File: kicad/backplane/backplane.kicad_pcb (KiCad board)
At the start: 2 copper layers, 190.5 x 105 mm, 56 parts, among them J1 Board Connector, J2 Board Connector, J3 Board Connector, J4 Board Connector, J5 Board Connector, J6 Board Connector, J7 Board Connector, J8 Conn_02x04_Counter_Clockwise, J9 Screw_Terminal_01x02, SW1 SW_SPDT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

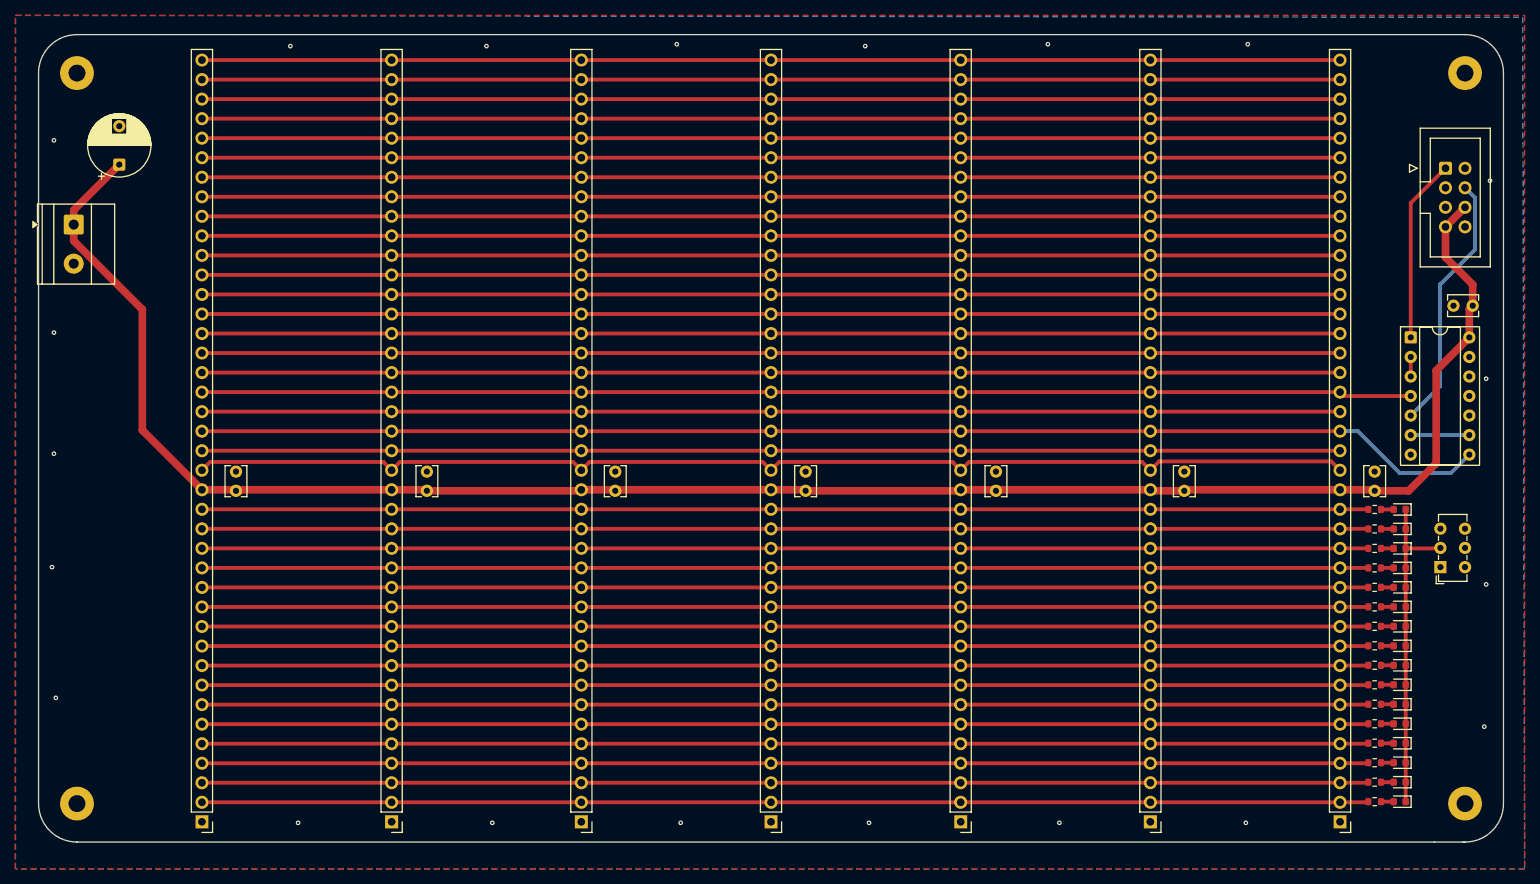
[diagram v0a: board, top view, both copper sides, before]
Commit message: integrated wozmon, updated kicad to specify phi1o
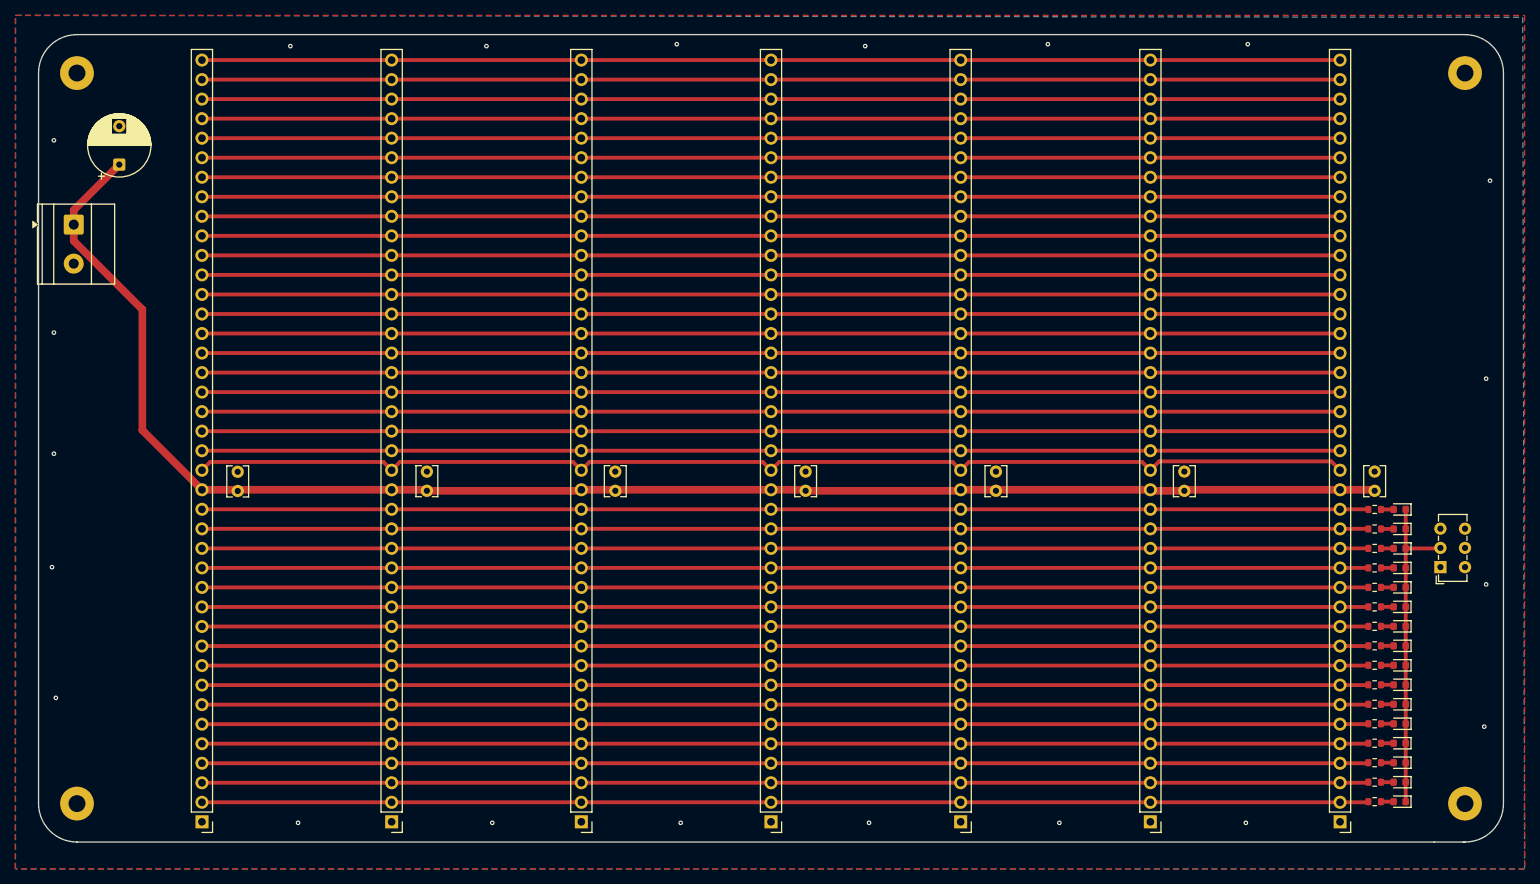
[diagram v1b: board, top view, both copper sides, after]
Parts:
- removed C9: 0.1u, Capacitor_THT:C_Disc_D3.8mm_W2.6mm_P2.50mm
- removed J8: Conn_02x04_Counter_Clockwise, Connector_IDC:IDC-Header_2x04_P2.54mm_Vertical
- removed U1: 7414, Package_DIP:DIP-14_W7.62mm_Socket
- moved C2 162.4 mm to (75.9, 104.3), turned to 90 degrees
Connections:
- net PHI2 renamed PHI1
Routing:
- net 5V: track 252.1 -> 204.9 mm
- net RESB_IN: track 33.6 -> 0.00 mm
- net PHI_IN: track 23.9 -> 0.00 mm
- net RESB: track 168.0 -> 148.0 mm
- net PHI1: track 157.4 -> 148.7 mm
- net Net-(U1-Pad6): track 7.62 -> 0.00 mm
- net Net-(U1-Pad2): track 2.54 -> 0.00 mm
